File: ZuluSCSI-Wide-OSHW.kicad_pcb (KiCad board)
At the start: 0 parts

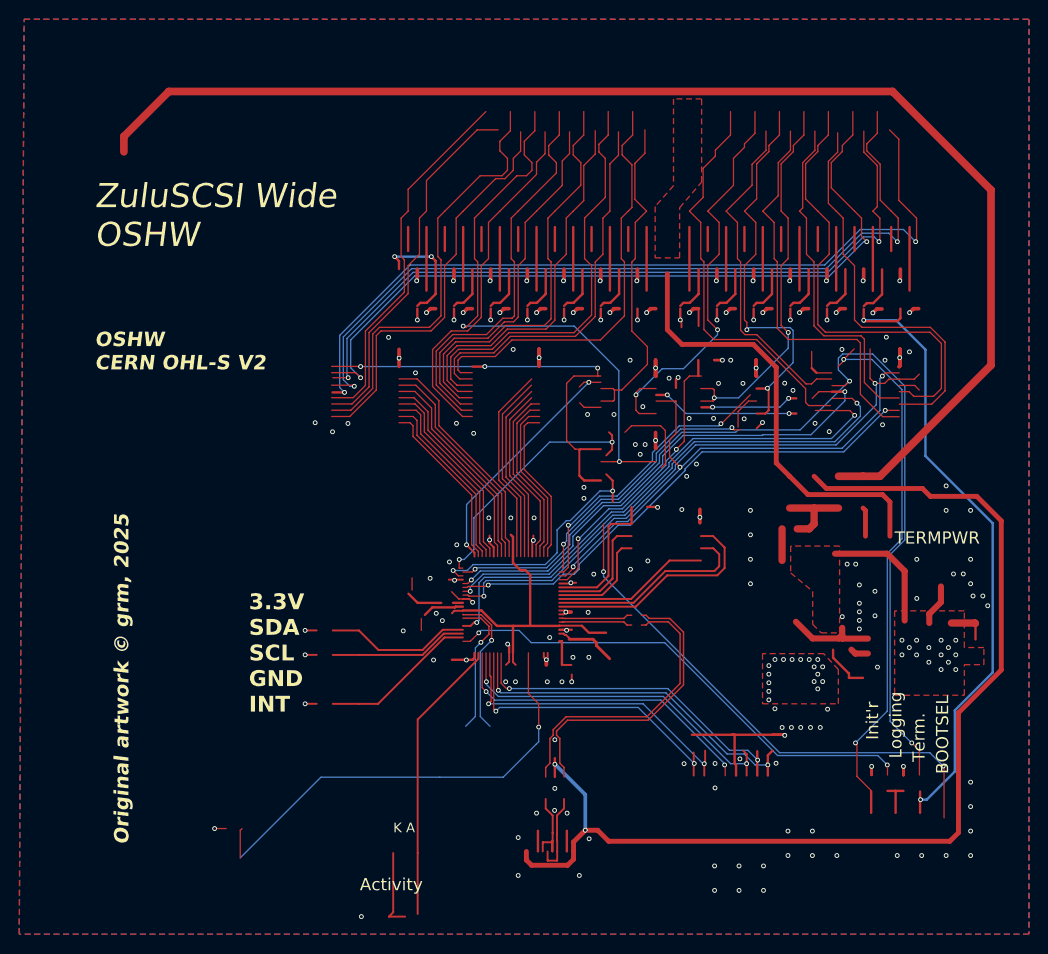
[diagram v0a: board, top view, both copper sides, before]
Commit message: Switch fonts, modify silkscreen
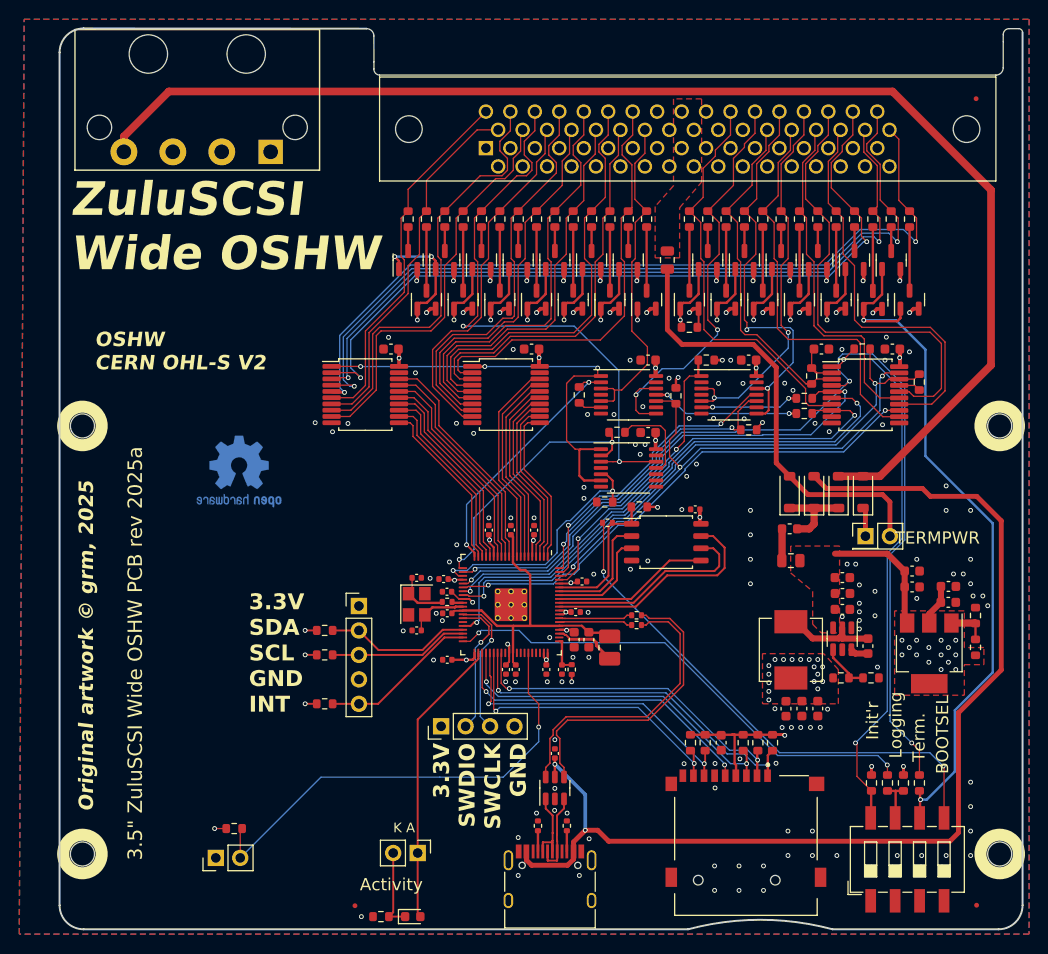
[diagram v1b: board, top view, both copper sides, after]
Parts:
- added C1: 100nF, Capacitor_SMD:C_0603_1608Metric, F.Cu at (95.5, 117.3)
- added C10: 100nF, Capacitor_SMD:C_0603_1608Metric, F.Cu at (115.4, 101.1)
- added C11: 100nF, Capacitor_SMD:C_0603_1608Metric, F.Cu at (119.1, 102.7)
- added C12: 22uF, Capacitor_SMD:C_0603_1608Metric, F.Cu at (105.6, 113.8)
- added C13: 22uF, Capacitor_SMD:C_0603_1608Metric, F.Cu at (103.9, 113.8)
- added C14: 100nF, Capacitor_SMD:C_0603_1608Metric, F.Cu at (110.8, 107.3)
- added C15: 10uF, Capacitor_SMD:C_0603_1608Metric, F.Cu at (108.1, 100.2)
- added C16: 100nF, Capacitor_SMD:C_0603_1608Metric, F.Cu at (102.3, 113.8)
- added C17: 1uF, Capacitor_SMD:C_0603_1608Metric, F.Cu at (108.1, 101.8)
- added C18: 100nF, Capacitor_SMD:C_0603_1608Metric, F.Cu at (108.1, 103.5)
- added C2: 12pF, Capacitor_SMD:C_0603_1608Metric, F.Cu at (105.9, 76.4)
- added C20: 22pF, Capacitor_SMD:C_0402_1005Metric, F.Cu at (63.9, 105.7)
- added C21: 22pF, Capacitor_SMD:C_0402_1005Metric, F.Cu at (63.9, 100.2)
- added C22: 100nF, Capacitor_SMD:C_0402_1005Metric, F.Cu at (74.2, 109.7)
- added C23: 4.7uF, Capacitor_SMD:C_0402_1005Metric, F.Cu at (67.1, 103.9)
- added C24: 100nF, Capacitor_SMD:C_0402_1005Metric, F.Cu at (73.7, 95.2)
- added C25: 1uF, Capacitor_SMD:C_0402_1005Metric, F.Cu at (80.4, 103.8)
- added C26: 4.7uF, Capacitor_SMD:C_0603_1608Metric, F.Cu at (80.3, 106.6)
- added C27: 100nF, Capacitor_SMD:C_0402_1005Metric, F.Cu at (76.1, 95.2)
- added C28: 100nF, Capacitor_SMD:C_0402_1005Metric, F.Cu at (71.4, 95.2)
- added C29: 100nF, Capacitor_SMD:C_0402_1005Metric, F.Cu at (66.7, 100.3)
- added C3: 100nF, Capacitor_SMD:C_0603_1608Metric, F.Cu at (113.3, 76.4)
- added C30: 100nF, Capacitor_SMD:C_0402_1005Metric, F.Cu at (67.1, 108.7)
- added C31: 100nF, Capacitor_SMD:C_0402_1005Metric, F.Cu at (73.2, 109.7)
- added C32: 100nF, Capacitor_SMD:C_0402_1005Metric, F.Cu at (77.4, 109.7)
- added C33: 100nF, Capacitor_SMD:C_0402_1005Metric, F.Cu at (78.3, 118.4)
- added C34: 100nF, Capacitor_SMD:C_0402_1005Metric, F.Cu at (92.8, 93.1)
- added C35: 4.7uF, Capacitor_SMD:C_0603_1608Metric, F.Cu at (81.8, 106.6)
- added C36: 4.7uF, Capacitor_SMD:C_0402_1005Metric, F.Cu at (79.0, 109.7)
- added C37: 100nF, Capacitor_SMD:C_0603_1608Metric, F.Cu at (61.2, 76.4)
- added C38: 100nF, Capacitor_SMD:C_0402_1005Metric, F.Cu at (81.1, 100.6)
- added C39: 100nF, Capacitor_SMD:C_0402_1005Metric, F.Cu at (67.1, 101.6)
- added C4: 100nF, Capacitor_SMD:C_0603_1608Metric, F.Cu at (75.8, 76.4)
- added C5: 100nF, Capacitor_SMD:C_0603_1608Metric, F.Cu at (87.9, 77.6)
- added C6: 100nF, Capacitor_SMD:C_0603_1608Metric, F.Cu at (98.4, 77.6)
- added C7: 100nF, Capacitor_SMD:C_0603_1608Metric, F.Cu at (87.9, 85.1)
- added C8: 1uF, Capacitor_SMD:C_0603_1608Metric, F.Cu at (115.4, 99.5)
- added C9: 1uF, Capacitor_SMD:C_0603_1608Metric, F.Cu at (119.1, 101.1)
- added D1: YELLOW, LED_SMD:LED_0603_1608Metric, F.Cu at (63.5, 135.4)
- added D2: D_Schottky, Diode_SMD:D_SOD-123, F.Cu at (110.3, 91.3)
- added D3: D_Schottky, Diode_SMD:D_SOD-123, F.Cu at (107.7, 91.3)
- added D4: D_Schottky, Diode_SMD:D_SOD-123, F.Cu at (102.6, 91.3)
- added D5: D_Schottky, Diode_SMD:D_SOD-123, F.Cu at (105.2, 91.3)
- added F1: 1A, Fuse:Fuse_0805_2012Metric, F.Cu at (89.9, 67.2)
- added F2: 1A, Fuse:Fuse_0805_2012Metric, F.Cu at (102.8, 98.4)
- added FID1: Fiducial, Fiducial:Fiducial_0.5mm_Mask1mm, F.Cu at (122.0, 134.2)
- added FID2: Fiducial, Fiducial:Fiducial_0.5mm_Mask1mm, F.Cu at (57.5, 134.2)
- added FID3: Fiducial, Fiducial:Fiducial_0.5mm_Mask1mm, F.Cu at (122.0, 50.4)
- added H1: ~, ZuluSCSI-Wide-OSHW:MH2.5_NPTH, F.Cu at (29.2, 84.4)
- added H2: ~, ZuluSCSI-Wide-OSHW:MH2.5_NPTH, F.Cu at (29.2, 128.9)
- added H3: ~, ZuluSCSI-Wide-OSHW:MH2.5_NPTH, F.Cu at (124.5, 84.4)
- added H4: ~, ZuluSCSI-Wide-OSHW:MH2.5_NPTH, F.Cu at (124.5, 128.9)
- added J1: USB_DATA, Connector_USB:USB_C_Receptacle_HRO_TYPE-C-31-M-12, F.Cu at (77.8, 132.7)
- added J2: TF003, ZuluSCSI-Wide-OSHW:TF01A, F.Cu at (98.1, 128.0)
- added J3: Conn_01x02, Connector_PinHeader_2.54mm:PinHeader_1x02_P2.54mm_Vertical, F.Cu at (64.0, 128.8)
- added J4: MnL, ZuluSCSI-Wide-OSHW:DRVPWR, F.Cu at (42.4, 61.0)
- added J5: HD68, ZuluSCSI-Wide-OSHW:5787169-7, F.Cu at (92.1, 54.5)
- added J6: Conn_01x05, Connector_PinHeader_2.54mm:PinHeader_1x05_P2.54mm_Vertical, F.Cu at (57.9, 103.1)
- added J7: Conn_01x04, Connector_PinHeader_2.54mm:PinHeader_1x04_P2.54mm_Vertical, F.Cu at (66.4, 115.6)
- added J8: Conn_01x02, Connector_PinHeader_2.54mm:PinHeader_1x02_P2.54mm_Vertical, F.Cu at (43.0, 129.3)
- added JP3: Jumper_2_Open, Connector_PinHeader_2.54mm:PinHeader_2x01_P2.54mm_Vertical, F.Cu at (110.5, 95.9)
- added L1: Ferrite_Bead_Small, Inductor_SMD:L_0603_1608Metric, F.Cu at (102.6, 95.1)
- added L2: 2.2uH, Inductor_SMD:L_Vishay_IHLP-2525, F.Cu at (102.8, 107.7)
- added L3: 3.3uH, Inductor_SMD:L_1008_2520Metric_Pad1.43x2.20mm_HandSolder, F.Cu at (83.9, 107.4)
- added Q1: AO3401A, Package_TO_SOT_SMD:SOT-23, F.Cu at (72.5, 71.3)
- added Q10: AO3401A, Package_TO_SOT_SMD:SOT-23, F.Cu at (92.2, 71.3)
- added Q11: AO3401A, Package_TO_SOT_SMD:SOT-23, F.Cu at (94.1, 67.2)
- added Q12: AO3401A, Package_TO_SOT_SMD:SOT-23, F.Cu at (96.0, 71.3)
- added Q13: AO3401A, Package_TO_SOT_SMD:SOT-23, F.Cu at (97.9, 67.2)
- added Q14: AO3401A, Package_TO_SOT_SMD:SOT-23, F.Cu at (99.8, 71.3)
- added Q15: AO3401A, Package_TO_SOT_SMD:SOT-23, F.Cu at (101.8, 67.2)
- added Q16: AO3401A, Package_TO_SOT_SMD:SOT-23, F.Cu at (103.7, 71.3)
- added Q17: AO3401A, Package_TO_SOT_SMD:SOT-23, F.Cu at (105.6, 67.2)
- added Q18: AO3401A, Package_TO_SOT_SMD:SOT-23, F.Cu at (107.5, 71.3)
- added Q19: AO3401A, Package_TO_SOT_SMD:SOT-23, F.Cu at (109.4, 67.2)
- added Q2: AO3401A, Package_TO_SOT_SMD:SOT-23, F.Cu at (74.5, 67.2)
- added Q20: AO3401A, Package_TO_SOT_SMD:SOT-23, F.Cu at (111.3, 71.3)
- added Q21: AO3401A, Package_TO_SOT_SMD:SOT-23, F.Cu at (113.2, 67.2)
- added Q22: AO3401A, Package_TO_SOT_SMD:SOT-23, F.Cu at (115.1, 71.3)
- added Q23: AO3401A, Package_TO_SOT_SMD:SOT-23, F.Cu at (63.0, 67.2)
- added Q24: AO3401A, Package_TO_SOT_SMD:SOT-23, F.Cu at (64.9, 71.3)
- added Q25: AO3401A, Package_TO_SOT_SMD:SOT-23, F.Cu at (66.8, 67.2)
- added Q26: AO3401A, Package_TO_SOT_SMD:SOT-23, F.Cu at (68.7, 71.3)
- added Q27: AO3401A, Package_TO_SOT_SMD:SOT-23, F.Cu at (70.6, 67.2)
- added Q3: AO3401A, Package_TO_SOT_SMD:SOT-23, F.Cu at (76.4, 71.3)
- added Q4: AO3401A, Package_TO_SOT_SMD:SOT-23, F.Cu at (78.3, 67.2)
- added Q5: AO3401A, Package_TO_SOT_SMD:SOT-23, F.Cu at (80.2, 71.3)
- added Q6: AO3401A, Package_TO_SOT_SMD:SOT-23, F.Cu at (82.1, 67.2)
- added Q7: AO3401A, Package_TO_SOT_SMD:SOT-23, F.Cu at (84.0, 71.3)
- added Q8: AO3401A, Package_TO_SOT_SMD:SOT-23, F.Cu at (85.9, 67.2)
- added Q9: AO3401A, Package_TO_SOT_SMD:SOT-23, F.Cu at (87.8, 71.3)
- added R1: 4k7, Resistor_SMD:R_0603_1608Metric, F.Cu at (100.9, 117.3)
- added R10: 4k7, Resistor_SMD:R_0603_1608Metric, F.Cu at (83.4, 92.3)
- added R11: 4k7, Resistor_SMD:R_0603_1608Metric, F.Cu at (90.8, 81.3)
- added R12: 4k7, Resistor_SMD:R_0603_1608Metric, F.Cu at (98.4, 84.8)
- added R13: 4k7, Resistor_SMD:R_0603_1608Metric, F.Cu at (94.0, 77.6)
- added R14: 1k, Resistor_SMD:R_0402_1005Metric, F.Cu at (67.1, 102.7)
- added R15: 4k7, Resistor_SMD:R_0603_1608Metric, F.Cu at (54.4, 105.7)
- added R16: 110, Resistor_SMD:R_0603_1608Metric, F.Cu at (104.9, 79.2)
- added R17: 1k, Resistor_SMD:R_0603_1608Metric, F.Cu at (116.1, 79.9)
- added R19: 1k, Resistor_SMD:R_0603_1608Metric, F.Cu at (80.8, 81.2)
- added R2: 4k7, Resistor_SMD:R_0603_1608Metric, F.Cu at (99.3, 117.3)
- added R20: 1k, Resistor_SMD:R_0603_1608Metric, F.Cu at (104.2, 81.6)
- added R21: 1k, Resistor_SMD:R_0603_1608Metric, F.Cu at (104.2, 83.1)
- added R22: 110, Resistor_SMD:R_0603_1608Metric, F.Cu at (72.5, 62.9)
- added R23: 110, Resistor_SMD:R_0603_1608Metric, F.Cu at (74.5, 62.9)
- added R24: 110, Resistor_SMD:R_0603_1608Metric, F.Cu at (76.4, 62.9)
- added R25: 110, Resistor_SMD:R_0603_1608Metric, F.Cu at (78.3, 62.9)
- added R26: 110, Resistor_SMD:R_0603_1608Metric, F.Cu at (80.2, 62.9)
- added R27: 110, Resistor_SMD:R_0603_1608Metric, F.Cu at (82.1, 62.9)
- added R28: 110, Resistor_SMD:R_0603_1608Metric, F.Cu at (84.0, 62.9)
- added R29: 110, Resistor_SMD:R_0603_1608Metric, F.Cu at (85.9, 62.9)
- added R3: 4k7, Resistor_SMD:R_0603_1608Metric, F.Cu at (97.8, 117.3)
- added R30: 110, Resistor_SMD:R_0603_1608Metric, F.Cu at (87.8, 62.9)
- added R31: 110, Resistor_SMD:R_0603_1608Metric, F.Cu at (92.2, 62.9)
- added R32: 110, Resistor_SMD:R_0603_1608Metric, F.Cu at (94.1, 62.9)
- added R33: 110, Resistor_SMD:R_0603_1608Metric, F.Cu at (96.0, 62.9)
- added R34: 110, Resistor_SMD:R_0603_1608Metric, F.Cu at (97.9, 62.9)
- added R35: 110, Resistor_SMD:R_0603_1608Metric, F.Cu at (99.8, 62.9)
- added R36: 110, Resistor_SMD:R_0603_1608Metric, F.Cu at (101.8, 62.9)
- added R37: 110, Resistor_SMD:R_0603_1608Metric, F.Cu at (103.7, 62.9)
- added R38: 110, Resistor_SMD:R_0603_1608Metric, F.Cu at (105.6, 62.9)
- added R39: 110, Resistor_SMD:R_0603_1608Metric, F.Cu at (107.5, 62.9)
- added R4: 1k, Resistor_SMD:R_0603_1608Metric, F.Cu at (111.1, 121.5)
- added R40: 4k7, Resistor_SMD:R_0603_1608Metric, F.Cu at (92.2, 74.2)
- added R41: 31k6, Resistor_SMD:R_0603_1608Metric, F.Cu at (108.0, 110.6)
- added R42: 10k, Resistor_SMD:R_0603_1608Metric, F.Cu at (111.1, 110.6)
- added R43: 4k7, Resistor_SMD:R_0603_1608Metric, F.Cu at (116.1, 121.5)
- added R44: ~, Resistor_SMD:R_0603_1608Metric, F.Cu at (121.9, 107.4)
- added R45: 0, Resistor_SMD:R_0603_1608Metric, F.Cu at (121.9, 104.1)
- added R46: 5k1, Resistor_SMD:R_0402_1005Metric, F.Cu at (79.5, 126.0)
- added R47: 5k1, Resistor_SMD:R_0402_1005Metric, F.Cu at (76.5, 126.0)
- added R48: 27, Resistor_SMD:R_0402_1005Metric, F.Cu at (86.7, 104.1)
- added R49: 27, Resistor_SMD:R_0402_1005Metric, F.Cu at (86.7, 105.1)
- added R5: 4k7, Resistor_SMD:R_0603_1608Metric, F.Cu at (93.9, 117.3)
- added R50: 510, Resistor_SMD:R_0603_1608Metric, F.Cu at (60.2, 135.4)
- added R51: 4k7, Resistor_SMD:R_0603_1608Metric, F.Cu at (54.4, 108.2)
- added R52: 4k7, Resistor_SMD:R_0603_1608Metric, F.Cu at (54.4, 113.3)
- added R53: 1k, Resistor_SMD:R_0402_1005Metric, F.Cu at (83.7, 94.5)
- added R54: 4k7, Resistor_SMD:R_0603_1608Metric, F.Cu at (87.0, 92.8)
- added R55: 110, Resistor_SMD:R_0603_1608Metric, F.Cu at (109.4, 62.9)
- added R56: 110, Resistor_SMD:R_0603_1608Metric, F.Cu at (111.3, 62.9)
- added R57: 110, Resistor_SMD:R_0603_1608Metric, F.Cu at (113.2, 62.9)
- added R58: 110, Resistor_SMD:R_0603_1608Metric, F.Cu at (115.1, 62.9)
- added R59: 110, Resistor_SMD:R_0603_1608Metric, F.Cu at (63.0, 62.9)
- added R6: 1k, Resistor_SMD:R_0603_1608Metric, F.Cu at (114.5, 121.5)
- added R60: 110, Resistor_SMD:R_0603_1608Metric, F.Cu at (64.9, 62.9)
- added R61: 110, Resistor_SMD:R_0603_1608Metric, F.Cu at (66.8, 62.9)
- added R62: 110, Resistor_SMD:R_0603_1608Metric, F.Cu at (68.7, 62.9)
- added R63: 110, Resistor_SMD:R_0603_1608Metric, F.Cu at (70.6, 62.9)
- added R64: 1k, Resistor_SMD:R_0603_1608Metric, F.Cu at (84.7, 85.1)
- added R65: 27, Resistor_SMD:R_0402_1005Metric, F.Cu at (80.0, 109.7)
- added R66: 4k7, Resistor_SMD:R_0603_1608Metric, F.Cu at (45.0, 126.2)
- added R7: 4k7, Resistor_SMD:R_0603_1608Metric, F.Cu at (92.3, 117.3)
- added R8: 4k7, Resistor_SMD:R_0603_1608Metric, F.Cu at (110.2, 76.4)
- added R9: 4k7, Resistor_SMD:R_0603_1608Metric, F.Cu at (112.8, 121.5)
- added REF**: OSHW-Logo2_9.8x8mm_Copper, Symbol:OSHW-Logo2_9.8x8mm_Copper, B.Cu at (45.5, 89.2)
- added SW1: SW_DIP_x04, Button_Switch_SMD:SW_DIP_SPSTx04_Slide_6.7x11.72mm_W8.61mm_P2.54mm_LowProfile, F.Cu at (114.9, 129.4)
- added U1: RP2350_80QFN, ZuluSCSI-Wide-OSHW:RP2350-QFN-80-1EP_10x10_P0.4mm_EP3.4x3.4mm_ThermalVias, F.Cu at (73.7, 103.0)
- added U10: W25Q128JVS, Package_SO:SOIC-8_5.23x5.23mm_P1.27mm, F.Cu at (89.8, 96.5)
- added U11: 74LVT245, Package_SO:SSOP-20_5.3x7.2mm_P0.65mm, F.Cu at (58.6, 81.2)
- added U2: 74LVT245, Package_SO:SSOP-20_5.3x7.2mm_P0.65mm, F.Cu at (73.2, 81.2)
- added U3: 74LVT245, Package_SO:SSOP-20_5.3x7.2mm_P0.65mm, F.Cu at (110.5, 81.2)
- added U4: 74LVT125, Package_SO:TSSOP-14_4.4x5mm_P0.65mm, F.Cu at (85.9, 88.8)
- added U5: 74LVT125, Package_SO:TSSOP-14_4.4x5mm_P0.65mm, F.Cu at (85.9, 81.2)
- added U6: 74LVT125, Package_SO:TSSOP-14_4.4x5mm_P0.65mm, F.Cu at (96.3, 81.2)
- added U7: AZ1117-2.85, Package_TO_SOT_SMD:SOT-223-3_TabPin2, F.Cu at (117.1, 108.0)
- added U8: AP62250WU, Package_TO_SOT_SMD:TSOT-23-6, F.Cu at (108.1, 106.5)
- added U9: USB TVS, Package_TO_SOT_SMD:SOT-23-6, F.Cu at (78.3, 122.0)
- added Y1: 12MHz, Crystal:Crystal_SMD_3225-4Pin_3.2x2.5mm, F.Cu at (63.9, 103.0)
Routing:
- net 35: track 197.2 -> 0.00 mm, vias 16 -> 0
- net /~{TERM_EN}: track 0.00 -> 197.2 mm, vias 0 -> 16
- net 88: track 179.2 -> 0.00 mm, vias 42 -> 0
- net +2V8: track 0.00 -> 179.2 mm, vias 0 -> 42
- net 7: track 136.6 -> 0.00 mm
- net /5V_IN: track 0.00 -> 136.6 mm
- net 9: track 115.1 -> 0.00 mm, vias 2 -> 0
- net /VBUS: track 0.00 -> 115.1 mm, vias 0 -> 2
- net 37: track 105.1 -> 0.00 mm, vias 3 -> 0
- net /~{MCU_REQ}: track 0.00 -> 105.1 mm, vias 0 -> 3
- net 108: track 86.0 -> 0.00 mm, vias 2 -> 0
- net /~{SCSI_SD10}: track 0.00 -> 86.0 mm, vias 0 -> 2
- net 109: track 85.1 -> 0.00 mm, vias 2 -> 0
- net /~{SCSI_SD11}: track 0.00 -> 85.1 mm, vias 0 -> 2
- net 106: track 81.4 -> 0.00 mm, vias 2 -> 0
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- added copper zone on F.Cu, net +2V8
- added copper zone on In2.Cu, net +2V8
- added copper zone on F.Cu, net +3V3
- added copper zone on In2.Cu, net +3V3
- added copper zone on F.Cu, net +5V
- added copper zone on F.Cu, net /TERMPWR
- added copper zone on B.Cu, net GND
- added copper zone on F.Cu, net GND
- added copper zone on In1.Cu, net GND
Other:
- board outline added: 100 x 93.5 mm
- copper layers 0 -> 4
- board text added: "3.3V SWDIO SWCLK GND"
- board text added: "3.5{dblquote} ZuluSCSI Wide OSHW PCB rev 2025a"

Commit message: Make board ZuluSCSI firmware compatible
The initial design of the Wide OSHW had pin differences that were
incompatible with unmodified ZuluSCSI firmware with wide support.

The following changes were made:
 - The BUS_DIR changed polarity in the wide firmware thus the A and B
 side on the data buffers had to be swapped

 - 74LVT125 could no longer be used to for the parity pins on the
 data bus. Thus one was replaced with a 74LVT245. Only two of the eight
 bus pins are used on the new 74LVT245. Maybe a different part would
 make sense

 - All the data and control signal buffers have had their VCC changed
 from the 3.3V power to 2.85V power. A section of the 3.3V power
 plane was replace with a 2.85 power plane to support this change

 - The I2C pin along with the interrupt pin have changed position
 to take advantage of the hardware I2C support and mirror their location
 in the wide firmware

 - The UF2 bootloader switch has been removed from the DIP switch
 and replaced with a momentary contact switch

 - The eject button footprint has been laid down

 - The OSHW logo is now a top solder mask

 - Fonts used in the design have now been embedded
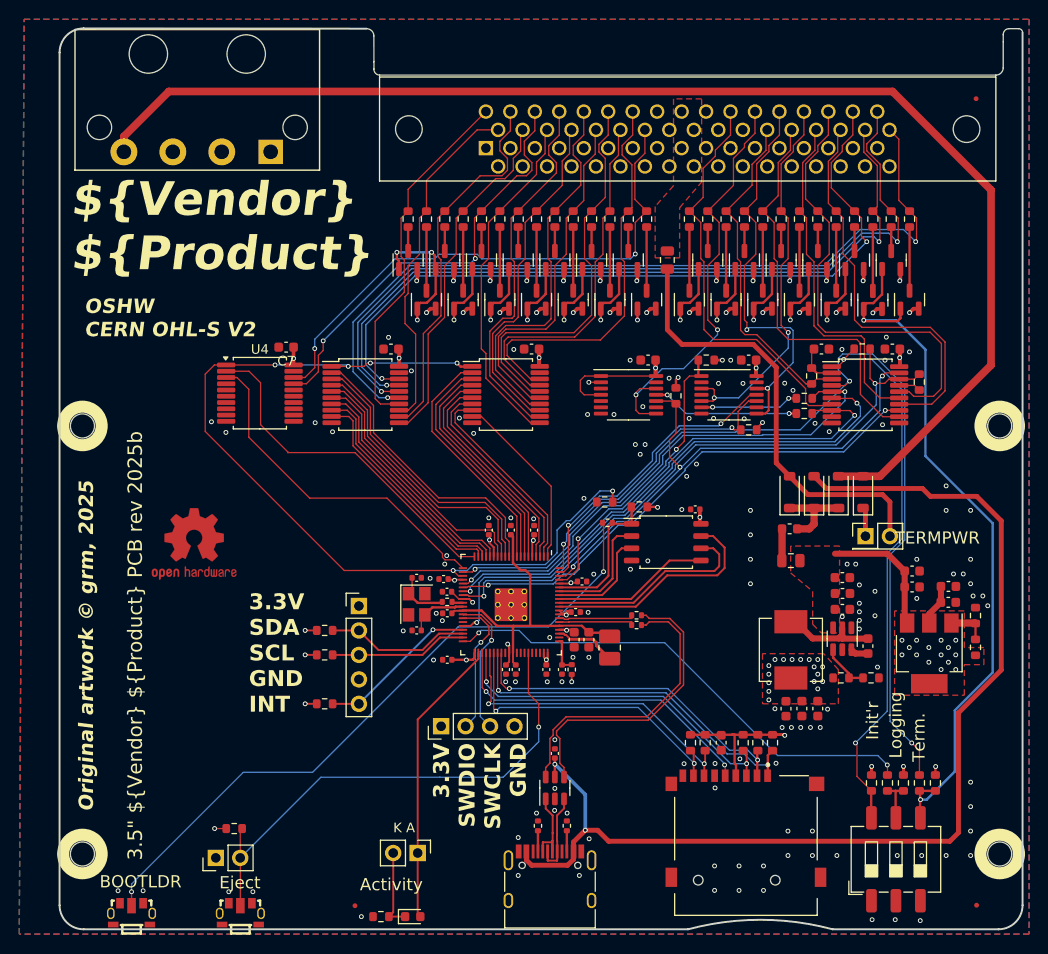
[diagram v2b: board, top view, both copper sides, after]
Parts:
- removed R19, R64: 1k, Resistor_SMD:R_0603_1608Metric
- removed R40: 4k7, Resistor_SMD:R_0603_1608Metric
- added R18: 1k, Resistor_SMD:R_0603_1608Metric, F.Cu at (117.8, 121.5)
- added SW2: SW_EJECT, ZuluSCSI-Wide-OSHW:SW-SMD_GT-TC108A-H034-L1S, F.Cu at (45.6, 135.1)
- added SW3: SW_BOOT, ZuluSCSI-Wide-OSHW:SW-SMD_GT-TC108A-H034-L1S, F.Cu at (34.3, 135.1)
- R43, R8: value 4k7 -> 2k
- REF**: moved to F.Cu
- SW1: value SW_DIP_x04 -> SW_DIP_x03; footprint Button_Switch_SMD:SW_DIP_SPSTx04_Slide_6.7x11.72mm_W8.61mm_P2.54mm_LowProfile -> Button_Switch_SMD:SW_DIP_SPSTx03_Slide_6.7x9.18mm_W8.61mm_P2.54mm_LowProfile
- U4: value 74LVT125 -> 74LVT245; footprint Package_SO:TSSOP-14_4.4x5mm_P0.65mm -> Package_SO:SSOP-20_5.3x7.2mm_P0.65mm
- moved U4 39.1 mm to (47.6, 81.0)
- moved C7 38.6 mm to (50.4, 76.2)
- moved REF** 8.85 mm to (40.8, 96.7), turned to 0 degrees
- moved SW1 1.19 mm to (113.7, 129.4)
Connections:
- C3 pad 1: +3V3 -> +2V8
- C37 pad 1: +3V3 -> +2V8
- C4 pad 1: +3V3 -> +2V8
- C5 pad 1: +3V3 -> +2V8
- C6 pad 1: +3V3 -> +2V8
- C7 pad 1: +3V3 -> +2V8
- R11 pad 1: +3V3 -> +2V8
- R12 pad 1: +3V3 -> +2V8
- R13 pad 1: +3V3 -> +2V8
- SW1 pad 4: GND -> /~{TERM_EN}
- SW1 pad 5: /~{USB_BOOT} -> Net-(R6-Pad2)
- SW1 pad 6: /~{TERM_EN} -> /~{INITIATOR}
- U1 pad 37: /I²C_SDA -> /I²C_INT
- U1 pad 38: /I²C_SCL -> /I²C_SDA
- U1 pad 39: /I²C_INT -> /I²C_SCL
- U11 pad 1: /~{BUS_DIR} -> /BUS_DIR
- U11 pad 11: /~{MCU_SD15} -> /~{SCSI_SD15}
- U11 pad 12: /~{MCU_SD14} -> /~{SCSI_SD14}
- U11 pad 13: /~{MCU_SD13} -> /~{SCSI_SD13}
- U11 pad 14: /~{MCU_SD12} -> /~{SCSI_SD12}
- U11 pad 15: /~{MCU_SD11} -> /~{SCSI_SD11}
- U11 pad 16: /~{MCU_SD10} -> /~{SCSI_SD10}
- U11 pad 17: /~{MCU_SD9} -> /~{SCSI_SD9}
- U11 pad 18: /~{MCU_SD8} -> /~{SCSI_SD8}
- U11 pad 2: /~{SCSI_SD8} -> /~{MCU_SD8}
- U11 pad 20: +3V3 -> +2V8
- U11 pad 3: /~{SCSI_SD9} -> /~{MCU_SD9}
- U11 pad 4: /~{SCSI_SD10} -> /~{MCU_SD10}
- U11 pad 5: /~{SCSI_SD11} -> /~{MCU_SD11}
- U11 pad 6: /~{SCSI_SD12} -> /~{MCU_SD12}
- U11 pad 7: /~{SCSI_SD13} -> /~{MCU_SD13}
- U11 pad 8: /~{SCSI_SD14} -> /~{MCU_SD14}
- U11 pad 9: /~{SCSI_SD15} -> /~{MCU_SD15}
- U2 pad 1: /~{BUS_DIR} -> /BUS_DIR
- U2 pad 11: /~{MCU_SD0} -> /~{SCSI_SD0}
- U2 pad 12: /~{MCU_SD1} -> /~{SCSI_SD1}
- U2 pad 13: /~{MCU_SD2} -> /~{SCSI_SD2}
- U2 pad 14: /~{MCU_SD3} -> /~{SCSI_SD3}
- U2 pad 15: /~{MCU_SD4} -> /~{SCSI_SD4}
- U2 pad 16: /~{MCU_SD5} -> /~{SCSI_SD5}
- U2 pad 17: /~{MCU_SD6} -> /~{SCSI_SD6}
- U2 pad 18: /~{MCU_SD7} -> /~{SCSI_SD7}
- U2 pad 2: /~{SCSI_SD7} -> /~{MCU_SD7}
- U2 pad 20: +3V3 -> +2V8
- U2 pad 3: /~{SCSI_SD6} -> /~{MCU_SD6}
- U2 pad 4: /~{SCSI_SD5} -> /~{MCU_SD5}
- U2 pad 5: /~{SCSI_SD4} -> /~{MCU_SD4}
- U2 pad 6: /~{SCSI_SD3} -> /~{MCU_SD3}
- U2 pad 7: /~{SCSI_SD2} -> /~{MCU_SD2}
- U2 pad 8: /~{SCSI_SD1} -> /~{MCU_SD1}
- U2 pad 9: /~{SCSI_SD0} -> /~{MCU_SD0}
- U3 pad 20: +3V3 -> +2V8
- U4 pad 1: /~{BUS_DIR} -> /BUS_DIR
- U4 pad 10: unconnected-(U4-Pad10) -> GND
- U4 pad 11: Net-(R64-Pad1) -> unconnected-(U4-B7-Pad11)
- U4 pad 12: /~{SCSI_SDP1} -> unconnected-(U4-B6-Pad12)
- U4 pad 13: GND -> unconnected-(U4-B5-Pad13)
- U4 pad 14: +3V3 -> unconnected-(U4-B4-Pad14)
- U4 pad 2: /~{MCU_SDP1} -> /~{MCU_SDP}
- U4 pad 3: /~{SCSI_SDP1} -> /~{MCU_SDP1}
- U4 pad 4: GND -> unconnected-(U4-A2-Pad4)
- U4 pad 5: /BUS_DIR -> unconnected-(U4-A3-Pad5)
- U4 pad 6: /~{BUS_DIR} -> unconnected-(U4-A4-Pad6)
- U4 pad 7: GND -> unconnected-(U4-A5-Pad7)
- U5 pad 1: /~{BUS_DIR} -> +2V8
- U5 pad 14: +3V3 -> +2V8
- U5 pad 2: /~{MCU_SDP} -> GND
- U5 pad 3: /~{SCSI_SDP} -> unconnected-(U5-Pad3)
- U5 pad 4: GND -> +2V8
- U5 pad 5: /~{SCSI_SDP} -> GND
- U5 pad 6: Net-(R19-Pad1) -> unconnected-(U5-Pad6)
- U6 pad 14: +3V3 -> +2V8
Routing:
- net +2V8: track 179.2 -> 70.6 mm, vias 42 -> 51
- net /BUS_DIR: track 25.8 -> 91.7 mm, vias 2 -> 6
- net /~{BUS_DIR}: track 48.8 -> 0.00 mm, vias 3 -> 0
- net /~{SCSI_SDP}: track 35.1 -> 57.2 mm, vias 0 -> 2
- net +3V3: track 70.1 -> 50.1 mm, vias 46 -> 38
- net /~{SCSI_SDP1}: track 60.6 -> 44.9 mm
- net /~{USB_BOOT}: track 54.3 -> 69.7 mm
- net /~{MCU_SDP}: track 26.2 -> 36.4 mm, vias 2 -> 0
- net /~{MCU_SDP1}: track 26.9 -> 35.9 mm, vias 2 -> 0
- net Net-(R64-Pad1): track 8.75 -> 0.00 mm
- net /~{MCU_SD10}: track 22.5 -> 28.6 mm
- net /~{MCU_SD9}: track 23.4 -> 29.4 mm
- net /~{SCSI_SD14}: track 45.2 -> 39.3 mm
- net /~{MCU_SD8}: track 24.3 -> 30.1 mm
- net /~{SCSI_SD15}: track 42.4 -> 36.6 mm
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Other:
- board text added: "${Vendor} ${Product}"
- board text added: "3.5{dblquote} ${Vendor} ${Product} PCB rev ${REVISION}"
- board text added: "BOOTLDR"
- board text added: "Eject"
- board text removed: "3.5{dblquote} ZuluSCSI Wide OSHW PCB rev 2025a"
- board text removed: "BOOTSEL"
- board text removed: "ZuluSCSI Wide OSHW"
